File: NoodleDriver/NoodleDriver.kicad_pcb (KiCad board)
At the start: 2 copper layers, 15 parts, among them J1 Conn_01x12, J2 Conn_01x12, U1 WS2811, U2 WS2811, U3 ULN2001, U4 74HC04

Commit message: Add a microcontroller, and regulator and USB-C connector.  Checkin before I try swapping out the microbit and 0.1" headers.  Part of #8
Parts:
- added C1: 1uF, Capacitor_SMD:C_0402_1005Metric, F.Cu at (161.8, 57.4)
- added C2: 1uF, Capacitor_SMD:C_0402_1005Metric, F.Cu at (169.4, 57.4)
- added C3: 10uF, Capacitor_SMD:C_0603_1608Metric, F.Cu at (172.5, 43.4)
- added C4: 10uF, Capacitor_SMD:C_0603_1608Metric, F.Cu at (168.9, 43.4)
- added C5: 0.1uF, Capacitor_SMD:C_0402_1005Metric, F.Cu at (172.0, 67.6)
- added C6: 0.1uF, Capacitor_SMD:C_0402_1005Metric, F.Cu at (205.5, 38.0)
- added C7: 1uF, Capacitor_SMD:C_0402_1005Metric, F.Cu at (176.3, 48.0)
- added C8: 1uF, Capacitor_SMD:C_0402_1005Metric, F.Cu at (179.3, 52.1)
- added D1: LED, LED_SMD:LED_0402_1005Metric, F.Cu at (170.7, 37.1)
- added D2: LED, LED_SMD:LED_0402_1005Metric, F.Cu at (168.1, 37.1)
- added J4: Conn_01x02_Socket, Connector_JST:JST_PH_B2B-PH-SM4-TB_1x02-1MP_P2.00mm_Vertical, F.Cu at (161.8, 35.8)
- added J5: USB_C_Receptacle_USB2.0_16P, USB-C-Paddle:USB_C_PADDLE, F.Cu at (195.0, 25.5)
- added R11: 2K, Resistor_SMD:R_0402_1005Metric, F.Cu at (174.2, 39.4)
- added R12: 22R, Resistor_SMD:R_0402_1005Metric, F.Cu at (196.8, 32.8)
- added R13: 22R, Resistor_SMD:R_0402_1005Metric, F.Cu at (193.8, 32.5)
- added R15: 5K1, Resistor_SMD:R_0402_1005Metric, F.Cu at (197.6, 28.4)
- added R16: 5K1, Resistor_SMD:R_0402_1005Metric, F.Cu at (192.5, 28.4)
- added R9: 560R, Resistor_SMD:R_0402_1005Metric, F.Cu at (173.2, 35.3)
- added U5: TP4057, Package_TO_SOT_SMD:TSOT-23-6, F.Cu at (170.6, 40.5)
- added U6: CH32V203F8U6, Package_DFN_QFN:QFN-20-1EP_3x3mm_P0.45mm_EP1.6x1.6mm, F.Cu at (205.1, 42.5)
- added U7: DS8242-33S3, Package_TO_SOT_SMD:SOT-23-3, F.Cu at (179.2, 49.0)
- moved R1 0.11 mm to (160.5, 57.4)
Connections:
- net Net-(U1-DIN) renamed PA10
- J3 pad 2: unconnected-(J3-Pad2) -> PA9
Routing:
- net GND: track 16.5 -> 60.5 mm, vias 1 -> 7
- net +BATT: track 98.6 -> 134.0 mm
- net VBUS: track 0.00 -> 26.7 mm, vias 0 -> 2
- net Net-(J5-D+-PadA6): track 0.00 -> 13.0 mm, vias 0 -> 1
- net Net-(J5-D--PadA7): track 0.00 -> 12.9 mm, vias 0 -> 2
- net Net-(J5-CC1): track 0.00 -> 4.16 mm
- net Net-(J5-CC2): track 0.00 -> 4.10 mm, vias 0 -> 1
- net Net-(D1-K): track 0.00 -> 3.82 mm
- net Net-(U1-VDD): track 0.00 -> 3.37 mm
- net Net-(U2-VDD): track 0.00 -> 3.31 mm
- net Net-(D2-K): track 0.00 -> 2.59 mm
- net Net-(U2-OUTB): track 7.72 -> 10.2 mm
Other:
- board outline added: 6.5 x 4.4 mm

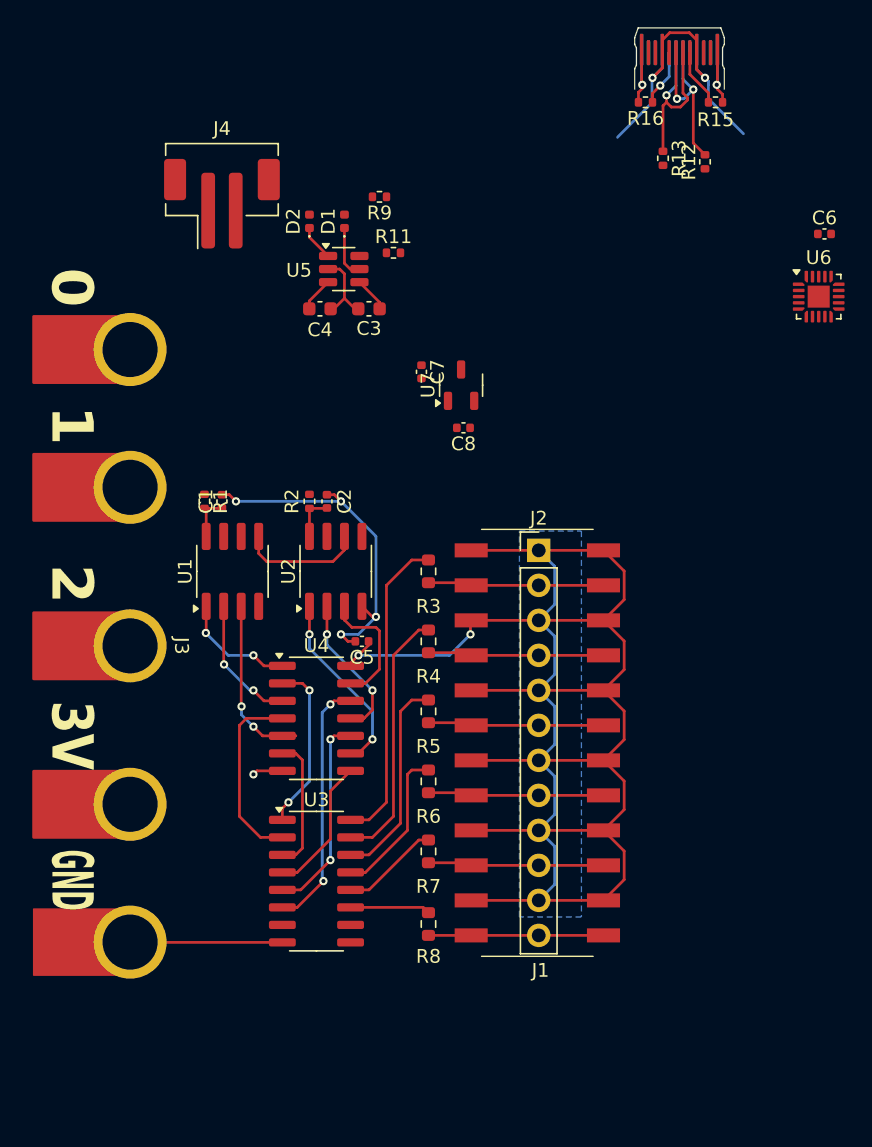
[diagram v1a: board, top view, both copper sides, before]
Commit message: Final tuning of prototype board, which we've ordered a handful of prototypes to be fabbed.  Part of #8
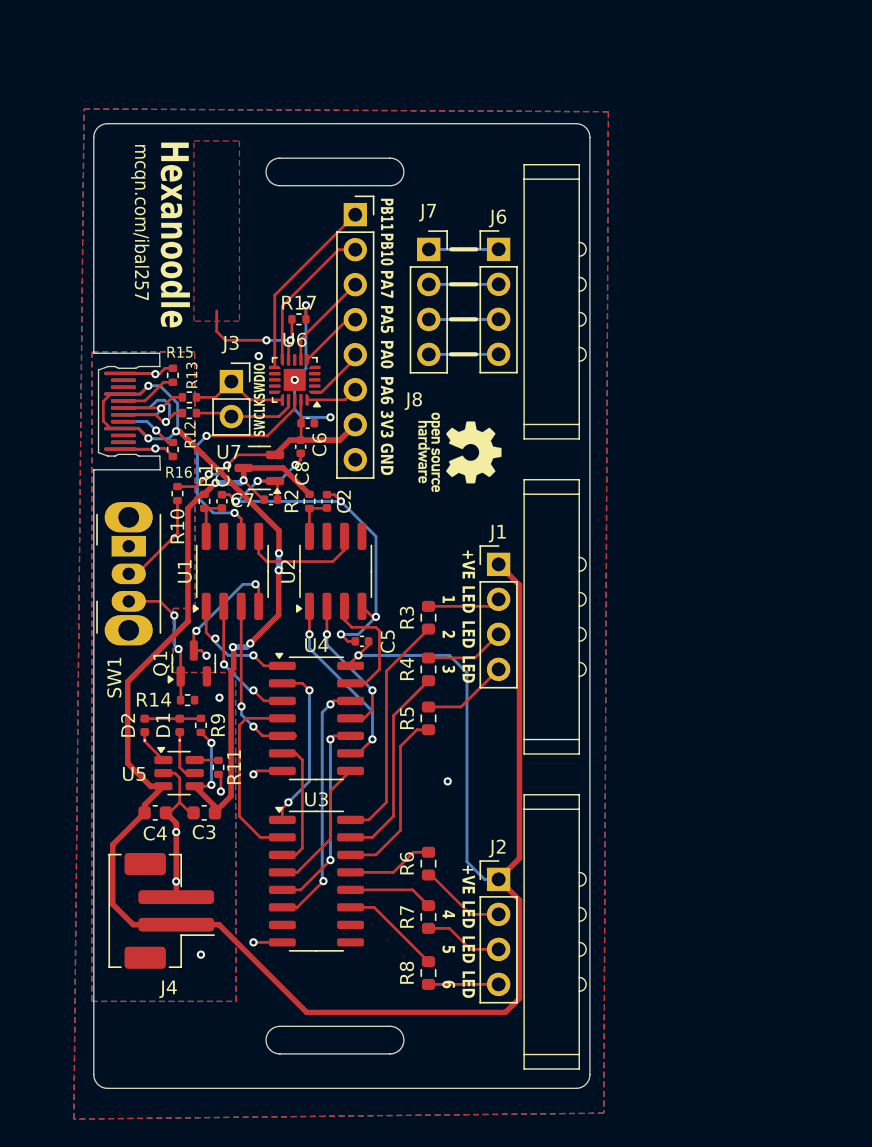
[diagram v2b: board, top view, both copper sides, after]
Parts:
- added J6: Conn_01x04, MagneticPogoPinConnector:MagneticPogoPinConnector_1x04_P2.54mm_Horizontal, F.Cu at (181.9, 39.1)
- added J7: Conn_01x04, Connector_PinSocket_2.54mm:PinSocket_1x04_P2.54mm_Vertical, F.Cu at (176.8, 39.1)
- added J8: Conn_01x08, Connector_PinSocket_2.54mm:PinSocket_1x08_P2.54mm_Vertical, F.Cu at (171.5, 36.6)
- added Q1: JSM2302, Package_TO_SOT_SMD:SOT-23, F.Cu at (159.8, 69.2)
- added R10: 10K, Resistor_SMD:R_0402_1005Metric, F.Cu at (158.6, 56.8)
- added R14: 100K, Resistor_SMD:R_0402_1005Metric, F.Cu at (159.3, 71.8)
- added R17: 1M, Resistor_SMD:R_0402_1005Metric, F.Cu at (167.4, 44.2)
- added REF**: OSHW-Logo_5.7x6mm_SilkScreen, Symbol:OSHW-Logo_5.7x6mm_SilkScreen, F.Cu at (179.1, 53.8)
- added REF**: WEEE-Logo_4.2x6mm_SilkScreen, Symbol:WEEE-Logo_4.2x6mm_SilkScreen, B.Cu at (157.2, 34.3)
- added SW1: On/Off, Button_Switch_THT:SW_Slide_SPDT_Angled_CK_OS102011MA1Q, F.Cu at (155.0, 60.7)
- J1: value Conn_01x12 -> Conn_01x04; footprint Connector-1x12-horizontal-smd:Connector-1x12-horizontal-smd -> MagneticPogoPinConnector:MagneticPogoPinConnector_1x04_P2.54mm_Horizontal
- J2: value Conn_01x12 -> Conn_01x04; footprint Connector_PinHeader_2.54mm:PinHeader_1x12_P2.54mm_Vertical -> MagneticPogoPinConnector:MagneticPogoPinConnector_1x04_P2.54mm_Horizontal
- J3: value ~ -> Conn_01x02; footprint Microbit-BoltConnector:Microbit Bolt Connector -> Connector_PinSocket_2.54mm:PinSocket_1x02_P2.54mm_Vertical
- moved J4 51.5 mm to (158.0, 87.1), turned to 90 degrees
- moved J5 47.1 mm to (155.3, 50.9), turned to 90 degrees
- moved R15 44.1 mm to (158.2, 48.3), turned to 90 degrees
- moved R16 42.6 mm to (158.2, 53.6), turned to -90 degrees
- moved R12 41.6 mm to (159.4, 51.0), turned to 0 degrees
- moved R9 40.5 mm to (160.3, 73.7), turned to 90 degrees
- moved C6 39.9 mm to (168.0, 51.7)
- moved R11 39.4 mm to (161.5, 76.7), turned to -90 degrees
- moved R13 38.5 mm to (159.4, 49.9), turned to 180 degrees
- moved U6 38.5 mm to (167.1, 48.6), turned to 180 degrees
- moved C3 38.5 mm to (160.5, 80.0)
- moved C4 38.5 mm to (157.0, 80.0)
- moved U5 38.5 mm to (158.7, 77.1)
- moved D1 38.5 mm to (158.7, 73.7)
- moved D2 38.5 mm to (156.2, 73.7)
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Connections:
- C3 pad 2: GND -> -BATT
- C4 pad 2: GND -> -BATT
- J1 pad 3: +BATT -> Net-(J1-Pin_3)
- J2 pad 2: Net-(J1-Pin_2) -> Net-(J2-Pin_2)
- J2 pad 3: +BATT -> Net-(J2-Pin_3)
- J2 pad 4: Net-(J1-Pin_4) -> Net-(J2-Pin_4)
- J3 pad 1: Net-(U2-DO) -> SWDIO
- J3 pad 2: PA9 -> SWCLK
- J4 pad 2: GND -> -BATT
- J5 pad A1: GND -> -BATT
- J5 pad A12: GND -> -BATT
- J5 pad B1: GND -> -BATT
- J5 pad B12: GND -> -BATT
- R11 pad 2: GND -> -BATT
- R12 pad 1: SWCLK -> Net-(J5-D--PadA7)
- R12 pad 2: Net-(J5-D--PadA7) -> SWCLK
- R13 pad 1: Net-(J5-D+-PadA6) -> SWDIO
- R13 pad 2: SWDIO -> Net-(J5-D+-PadA6)
- R15 pad 2: GND -> -BATT
- R16 pad 2: GND -> -BATT
- R4 pad 2: Net-(J1-Pin_4) -> Net-(J1-Pin_3)
- R5 pad 2: Net-(J1-Pin_6) -> Net-(J1-Pin_4)
- R6 pad 2: Net-(J1-Pin_8) -> Net-(J2-Pin_2)
- R7 pad 2: Net-(J1-Pin_10) -> Net-(J2-Pin_3)
- R8 pad 2: Net-(J1-Pin_12) -> Net-(J2-Pin_4)
- U2 pad 5: Net-(U2-DO) -> unconnected-(U2-DO-Pad5)
- U5 pad 2: GND -> -BATT
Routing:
- net VBUS: track 26.7 -> 62.0 mm, vias 2 -> 9
- net -BATT: track 0.00 -> 27.6 mm, vias 0 -> 7
- net +3V3: track 0.00 -> 17.7 mm, vias 0 -> 2
- net PA10: track 0.00 -> 17.7 mm, vias 0 -> 2
- net PB11: track 0.00 -> 13.5 mm
- net Net-(J1-Pin_6): track 12.8 -> 0.00 mm
- net Net-(J1-Pin_8): track 12.8 -> 0.00 mm
- net Net-(J1-Pin_10): track 12.8 -> 0.00 mm
- net Net-(J1-Pin_12): track 12.7 -> 0.00 mm
- net PB10: track 0.00 -> 10.9 mm
- net PB1: track 0.00 -> 10.4 mm, vias 0 -> 2
- net Net-(Q1-G): track 0.00 -> 9.65 mm, vias 0 -> 2
- net SWCLK: track 0.00 -> 7.59 mm
- net Net-(J1-Pin_2): track 12.8 -> 5.30 mm
- net SWDIO: track 0.00 -> 7.26 mm
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- added copper zone on B.Cu, net -BATT
- added copper zone on F.Cu, net -BATT
- added copper zone on B.Cu, net GND
- added copper zone on F.Cu, net GND
- added copper zone on F.Cu, net PB1
- removed copper zone on B.Cu, net +BATT
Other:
- board size 6.5 x 4.4 mm -> 36 x 70 mm
- board text added: "+VE"
- board text added: "3V3"
- board text added: "GND"
- board text added: "Hexanoodle"
- board text added: "LED 1"
- board text added: "LED 2"
- board text added: "LED 3"
- board text added: "LED 4"
- board text added: "LED 5"
- board text added: "LED 6"
- board text added: "PA0"
- board text added: "PA5"
- board text added: "PA6"
- board text added: "PA7"
- board text added: "PB10"
- board text added: "PB11"
- board text added: "SWCLK"
- board text added: "SWDIO"
- board text added: "mcqn.com/ibal257"
- board text added: "r20250924"
